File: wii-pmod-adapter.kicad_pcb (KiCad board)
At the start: 2 copper layers, 22 parts, among them J1 Conn_02x06_Odd_Even, J2 Conn_02x06_Odd_Even, J3 PWR, J4 DATA, J5 CLK, J6 MISC

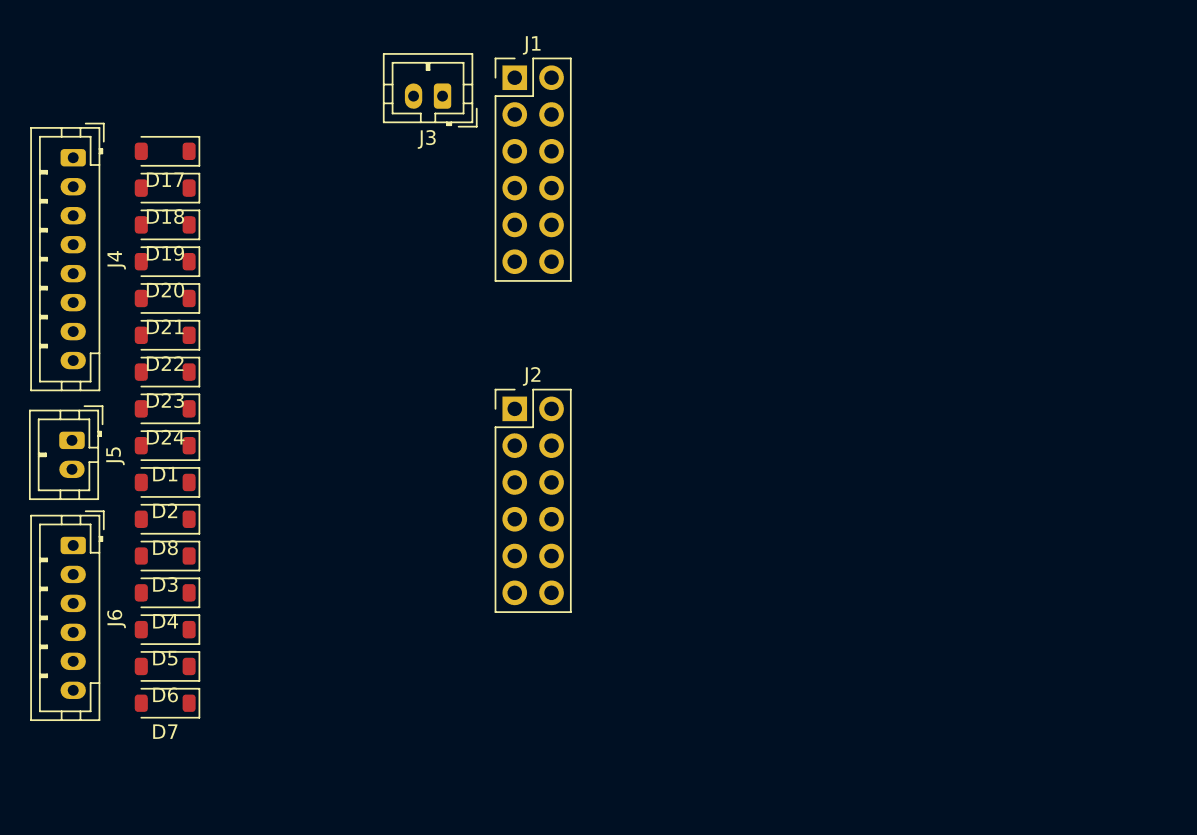
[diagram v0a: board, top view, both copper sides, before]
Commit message: Routed PMOD1
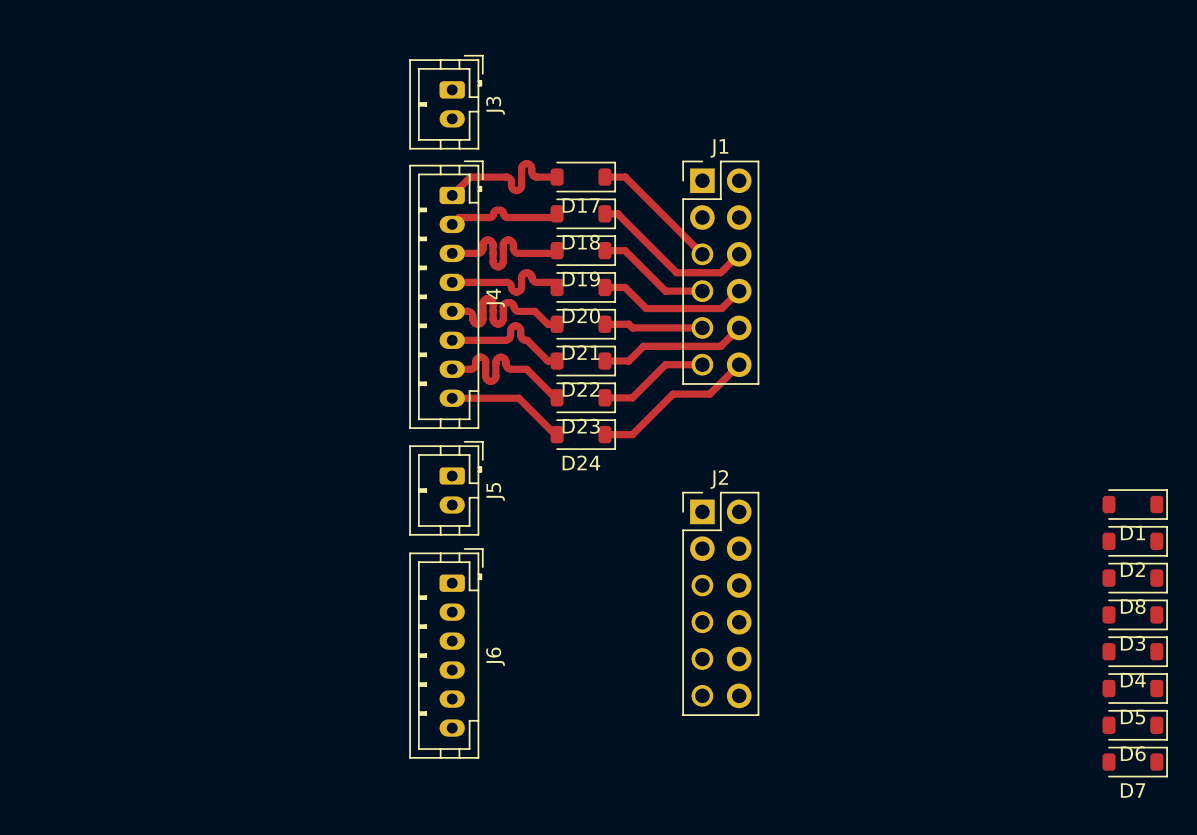
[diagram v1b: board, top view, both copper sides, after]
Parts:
- moved D1 66.9 mm to (96.0, 44.7)
- moved D2 66.9 mm to (96.0, 47.2)
- moved D3 66.9 mm to (96.0, 52.3)
- moved D4 66.9 mm to (96.0, 54.9)
- moved D5 66.9 mm to (96.0, 57.4)
- moved D6 66.9 mm to (96.0, 59.9)
- moved D7 66.9 mm to (96.0, 62.5)
- moved D8 66.9 mm to (96.0, 49.8)
- moved D18 28.8 mm to (57.9, 24.6)
- moved D19 28.8 mm to (57.9, 27.2)
- moved D21 28.8 mm to (57.9, 32.3)
- moved D17 28.8 mm to (57.9, 22.1)
- moved D20 28.8 mm to (57.9, 29.7)
- moved D22 28.8 mm to (57.9, 34.8)
- moved D23 28.8 mm to (57.9, 37.3)
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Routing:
- net Net-(D21-A): track 0.00 -> 12.5 mm
- net Net-(D23-A): track 0.00 -> 11.8 mm
- net Net-(D19-A): track 0.00 -> 11.6 mm
- net IO1: track 0.00 -> 11.5 mm
- net IO7: track 0.00 -> 11.3 mm
- net Net-(D17-A): track 0.00 -> 10.5 mm
- net IO3: track 0.00 -> 10.4 mm
- net IO5: track 0.00 -> 10.2 mm
- net Net-(D22-A): track 0.00 -> 9.18 mm
- net Net-(D20-A): track 0.00 -> 9.10 mm
- net IO0: track 0.00 -> 8.94 mm
- net Net-(D24-A): track 0.00 -> 8.28 mm
- net Net-(D18-A): track 0.00 -> 8.08 mm
- net IO2: track 0.00 -> 7.89 mm
- net IO6: track 0.00 -> 7.68 mm
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
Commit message: Routing done
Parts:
- moved D1 106.2 mm to (13.5, -22.1)
- moved D2 106.2 mm to (13.5, -19.6)
- moved D3 106.2 mm to (13.5, -14.5)
- moved D4 106.2 mm to (13.5, -12.0)
- moved D5 106.2 mm to (13.5, -9.41)
- moved D6 106.2 mm to (13.5, -6.87)
- moved D7 106.2 mm to (13.5, -4.33)
- moved D8 106.2 mm to (13.5, -17.0)
- moved D17 79.8 mm to (13.5, -44.2)
- moved D18 79.8 mm to (13.5, -41.7)
- moved D19 79.8 mm to (13.5, -39.1)
- moved D20 79.8 mm to (13.5, -36.6)
- moved D21 79.8 mm to (13.5, -34.1)
- moved D22 79.8 mm to (13.5, -31.5)
- moved D23 79.8 mm to (13.5, -29.0)
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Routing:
- net GND: track 0.00 -> 25.2 mm
- net +3V3: track 0.00 -> 24.9 mm
- net IO9: track 0.00 -> 11.7 mm
- net IO15: track 0.00 -> 11.0 mm
- net Net-(D1-A): track 0.00 -> 10.9 mm
- net IO11: track 0.00 -> 10.7 mm
- net IO13: track 0.00 -> 9.90 mm
- net IO8: track 0.00 -> 9.26 mm
- net Net-(D8-A): track 0.00 -> 8.31 mm
- net IO10: track 0.00 -> 8.20 mm
- net Net-(D2-A): track 0.00 -> 8.17 mm
- net Net-(D3-A): track 0.00 -> 8.09 mm
- net Net-(D4-A): track 0.00 -> 7.86 mm
- net Net-(D5-A): track 0.00 -> 7.64 mm
- net Net-(D6-A): track 0.00 -> 7.42 mm
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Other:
- board outline added: 25.4 x 51.1 mm
